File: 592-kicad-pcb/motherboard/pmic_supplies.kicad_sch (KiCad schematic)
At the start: 16 parts, among them J20 Conn_01x03, J21 Conn_01x03, J22 Conn_01x03, U21 MICROCHIP TC1304-VI0EMF, U22 LT1761ES5-BYPTRMPBF

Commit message: updates to routing
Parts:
- renumbered C39 to C42, C36 to C43, C40 to C44, C37 to C45, C38 to C46, C41 to C47, J20 to J28, J21 to J29, J22 to J30, JP5 to JP3, JP3 to JP5, R58 to R59, U21 to U22, U22 to U23
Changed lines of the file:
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@@
 		(on_board yes)
 		(dnp no)
-		(property "Reference" "U22"
+		(property "Reference" "U23"
 			(at 114.046 111.76 0)
 			(effects
@@
 			(project ""
 				(path "/5b0c97ac-fa03-4db8-b41b-0eee32b6f55d/f049e4ad-bebe-4338-850a-2727de737ae9/5cd7239b-a735-4cd0-9e02-9ed9ef16f904"
-					(reference "U22")
+					(reference "U23")
 					(unit 1)
 				)
@@
 		(on_board yes)
 		(dnp no)
-		(property "Reference" "C39"
+		(property "Reference" "C42"
 			(at 83.82 105.4035 0)
 			(effects
@@
 			(project "motherboard"
 				(path "/5b0c97ac-fa03-4db8-b41b-0eee32b6f55d/f049e4ad-bebe-4338-850a-2727de737ae9/5cd7239b-a735-4cd0-9e02-9ed9ef16f904"
-					(reference "C39")
+					(reference "C42")
 					(unit 1)
 				)
@@
 		(on_board yes)
 		(dnp no)
-		(property "Reference" "J22"
+		(property "Reference" "J30"
 			(at 199.39 105.4099 0)
 			(effects
@@
 			(project "motherboard"
 				(path "/5b0c97ac-fa03-4db8-b41b-0eee32b6f55d/f049e4ad-bebe-4338-850a-2727de737ae9/5cd7239b-a735-4cd0-9e02-9ed9ef16f904"
-					(reference "J22")
+					(reference "J30")
 					(unit 1)
 				)
@@
 		(on_board yes)
 		(dnp no)
-		(property "Reference" "C41"
+		(property "Reference" "C47"
 			(at 157.48 105.4035 0)
 			(effects
@@
 			(project "motherboard"
 				(path "/5b0c97ac-fa03-4db8-b41b-0eee32b6f55d/f049e4ad-bebe-4338-850a-2727de737ae9/5cd7239b-a735-4cd0-9e02-9ed9ef16f904"
-					(reference "C41")
+					(reference "C47")
 					(unit 1)
 				)
@@
 		(on_board yes)
 		(dnp no)
-		(property "Reference" "C40"
+		(property "Reference" "C44"
 			(at 139.7 105.4035 0)
 			(effects
@@
 			(project "motherboard"
 				(path "/5b0c97ac-fa03-4db8-b41b-0eee32b6f55d/f049e4ad-bebe-4338-850a-2727de737ae9/5cd7239b-a735-4cd0-9e02-9ed9ef16f904"
-					(reference "C40")
+					(reference "C44")
 					(unit 1)
 				)
@@
 		(on_board yes)
 		(dnp no)
-		(property "Reference" "R58"
+		(property "Reference" "R59"
 			(at 142.24 57.1499 0)
 			(effects
@@
 			(project ""
 				(path "/5b0c97ac-fa03-4db8-b41b-0eee32b6f55d/f049e4ad-bebe-4338-850a-2727de737ae9/5cd7239b-a735-4cd0-9e02-9ed9ef16f904"
-					(reference "R58")
+					(reference "R59")
 					(unit 1)
 				)
@@
 		(dnp no)
 		(fields_autoplaced yes)
-		(property "Reference" "JP5"
+		(property "Reference" "JP3"
 			(at 170.18 31.75 0)
 			(effects
@@
 			(project "motherboard"
 				(path "/5b0c97ac-fa03-4db8-b41b-0eee32b6f55d/f049e4ad-bebe-4338-850a-2727de737ae9/5cd7239b-a735-4cd0-9e02-9ed9ef16f904"
-					(reference "JP5")
+					(reference "JP3")
 					(unit 1)
 				)
@@
 		(on_board yes)
 		(dnp no)
-		(property "Reference" "C37"
+		(property "Reference" "C45"
 			(at 157.48 44.4565 0)
 			(effects
@@
 			(project "motherboard"
 				(path "/5b0c97ac-fa03-4db8-b41b-0eee32b6f55d/f049e4ad-bebe-4338-850a-2727de737ae9/5cd7239b-a735-4cd0-9e02-9ed9ef16f904"
-					(reference "C37")
+					(reference "C45")
 					(unit 1)
 				)
@@
 		(on_board yes)
 		(dnp no)
-		(property "Reference" "J21"
+		(property "Reference" "J29"
 			(at 199.39 52.0699 0)
 			(effects
@@
 			(project "motherboard"
 				(path "/5b0c97ac-fa03-4db8-b41b-0eee32b6f55d/f049e4ad-bebe-4338-850a-2727de737ae9/5cd7239b-a735-4cd0-9e02-9ed9ef16f904"
-					(reference "J21")
+					(reference "J29")
 					(unit 1)
 				)
@@
 		(on_board yes)
 		(dnp no)
-		(property "Reference" "J20"
+		(property "Reference" "J28"
 			(at 199.39 39.3699 0)
 			(effects
@@
 			(project "motherboard"
 				(path "/5b0c97ac-fa03-4db8-b41b-0eee32b6f55d/f049e4ad-bebe-4338-850a-2727de737ae9/5cd7239b-a735-4cd0-9e02-9ed9ef16f904"
-					(reference "J20")
+					(reference "J28")
 					(unit 1)
 				)
@@
 		(on_board yes)
 		(dnp no)
-		(property "Reference" "C36"
+		(property "Reference" "C43"
 			(at 86.36 39.3635 0)
 			(effects
@@
 			(project ""
 				(path "/5b0c97ac-fa03-4db8-b41b-0eee32b6f55d/f049e4ad-bebe-4338-850a-2727de737ae9/5cd7239b-a735-4cd0-9e02-9ed9ef16f904"
-					(reference "C36")
+					(reference "C43")
 					(unit 1)
 				)
@@
 		(dnp no)
 		(fields_autoplaced yes)
-		(property "Reference" "JP3"
+		(property "Reference" "JP5"
 			(at 172.72 97.79 0)
 			(effects
@@
 			(project ""
 				(path "/5b0c97ac-fa03-4db8-b41b-0eee32b6f55d/f049e4ad-bebe-4338-850a-2727de737ae9/5cd7239b-a735-4cd0-9e02-9ed9ef16f904"
-					(reference "JP3")
+					(reference "JP5")
 					(unit 1)
 				)
@@
 		(on_board yes)
 		(dnp no)
-		(property "Reference" "U21"
+		(property "Reference" "U22"
 			(at 114.3 44.958 0)
 			(effects
@@
 			(project ""
 				(path "/5b0c97ac-fa03-4db8-b41b-0eee32b6f55d/f049e4ad-bebe-4338-850a-2727de737ae9/5cd7239b-a735-4cd0-9e02-9ed9ef16f904"
-					(reference "U21")
+					(reference "U22")
 					(unit 1)
 				)
@@
 		(on_board yes)
 		(dnp no)
-		(property "Reference" "C38"
+		(property "Reference" "C46"
 			(at 157.48 54.6165 0)
 			(effects
@@
 			(project "motherboard"
 				(path "/5b0c97ac-fa03-4db8-b41b-0eee32b6f55d/f049e4ad-bebe-4338-850a-2727de737ae9/5cd7239b-a735-4cd0-9e02-9ed9ef16f904"
-					(reference "C38")
-					(unit 1)
-				)
+					(reference "C46")
+					(unit 1)
+				)

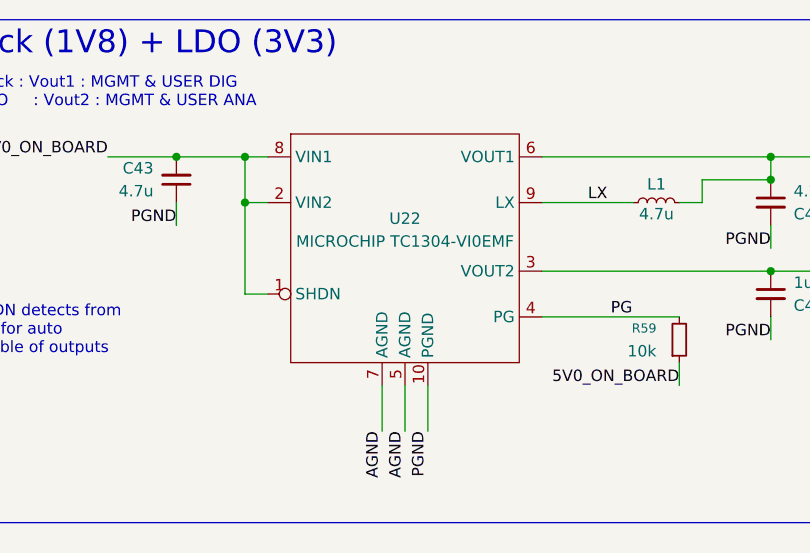
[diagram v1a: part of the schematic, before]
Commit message: update jlcpcb part numbers
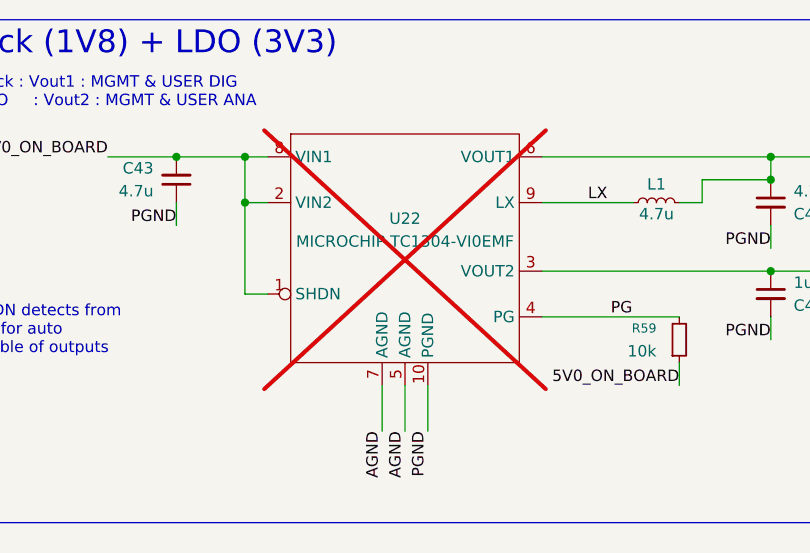
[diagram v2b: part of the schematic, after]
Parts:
- U22: now not fitted
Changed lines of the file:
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@@
 		(in_bom yes)
 		(on_board yes)
-		(dnp no)
+		(dnp yes)
 		(property "Reference" "U22"
 			(at 114.3 44.958 0)

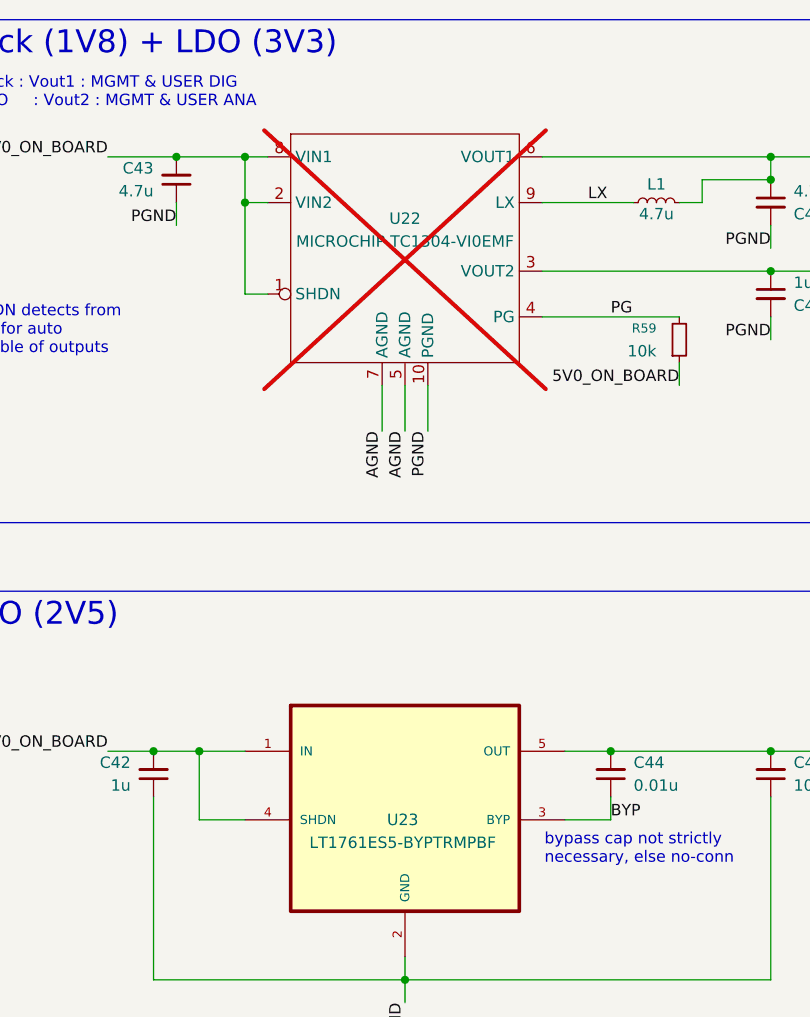
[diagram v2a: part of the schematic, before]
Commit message: can't work on one machine
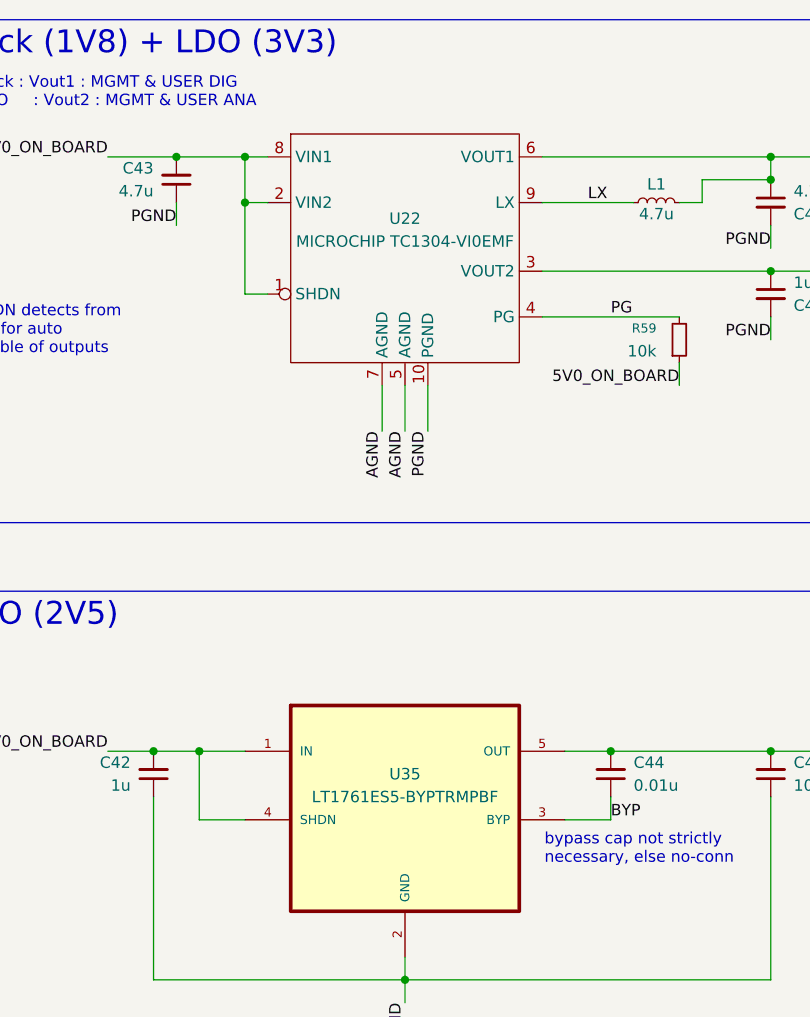
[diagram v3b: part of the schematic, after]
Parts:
- removed U23: LT1761ES5-BYPTRMPBF, LT1761ES5-BYPTRMPBF:SOT95P280X145-5N, symbol LT1761ES5-BYPTRMPBF:LT1761ES5-BYPTRMPBF
- added U35: LT1761ES5-BYPTRMPBF, LT1761ES5-BYPTRMPBF:SOT95P280X145-5N, symbol 592-partslib:LT1761ES5-BYPTRMPBF
- C43, C45: footprint (none) -> Capacitor_Tantalum_SMD:CP_EIA-3216-18_Kemet-A; LCSC (none) -> C7187
- U22: footprint (none) -> Package_DFN_QFN:DFN-10-1EP_3x3mm_P0.5mm_EP1.55x2.48mm; LCSC (none) -> C635408; now fitted; now left out of the parts list
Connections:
- net 5V0_ON_BOARD: now also U35.1 (IN), U35.4 (SHDN)
- net BYP: now also U35.3 (BYP)
- net GND: now also U35.2 (GND)
- net at C44.2, C47.2, JP5.1 (A): now also U35.5 (OUT)
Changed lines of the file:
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@@
-	)
-	(symbol
-		(lib_id "LT1761ES5-BYPTRMPBF:LT1761ES5-BYPTRMPBF")
-		(at 114.3 106.68 0)
-		(unit 1)
-		(exclude_from_sim no)
-		(in_bom yes)
-		(on_board yes)
-		(dnp no)
-		(property "Reference" "U23"
-			(at 114.046 111.76 0)
-			(effects
-				(font
-					(size 1.27 1.27)
-				)
-			)
-		)
-		(property "Value" "LT1761ES5-BYPTRMPBF"
-			(at 114.046 114.3 0)
-			(effects
-				(font
-					(size 1.27 1.27)
-				)
-			)
-		)
-		(property "Footprint" "LT1761ES5-BYPTRMPBF:SOT95P280X145-5N"
-			(at 114.3 106.68 0)
-			(effects
-				(font
-					(size 1.27 1.27)
-				)
-				(justify bottom)
-				(hide yes)
-			)
-		)
-		(property "Datasheet" "https://www.analog.com/media/en/technical-documentation/data-sheets/1761sff.pdf"
-			(at 114.3 106.68 0)
-			(effects
-				(font
-					(size 1.27 1.27)
-				)
-				(hide yes)
-			)
-		)
-		(property "Description" "Fixed 2V5 100mA LDO"
-			(at 114.3 106.68 0)
-			(effects
-				(font
-					(size 1.27 1.27)
-				)
-				(hide yes)
-			)
-		)
-		(property "MPN" "LT1761ES5-BYP#TRMPBF"
-			(at 114.3 106.68 0)
-			(effects
-				(font
-					(size 1.27 1.27)
-				)
-				(justify bottom)
-				(hide yes)
-			)
-		)
-		(property "SUPPLIER" "Linear Technology"
-			(at 114.3 106.68 0)
-			(effects
-				(font
-					(size 1.27 1.27)
-				)
-				(justify bottom)
-				(hide yes)
-			)
-		)
-		(property "OC_NEWARK" "19P0914"
-			(at 114.3 106.68 0)
-			(effects
-				(font
-					(size 1.27 1.27)
-				)
-				(justify bottom)
-				(hide yes)
-			)
-		)
-		(property "OC_FARNELL" "1663782"
-			(at 114.3 106.68 0)
-			(effects
-				(font
-					(size 1.27 1.27)
-				)
-				(justify bottom)
-				(hide yes)
-			)
-		)
-		(property "PACKAGE" "SOT-23-5"
-			(at 114.3 106.68 0)
-			(effects
-				(font
-					(size 1.27 1.27)
-				)
-				(justify bottom)
-				(hide yes)
-			)
-		)
-		(pin "4"
-		)
-		(pin "1"
-		)
-		(pin "5"
-		)
-		(pin "3"
-		)
-		(pin "2"
-		)
-		(instances
-			(project ""
-				(path "/5b0c97ac-fa03-4db8-b41b-0eee32b6f55d/f049e4ad-bebe-4338-850a-2727de737ae9/5cd7239b-a735-4cd0-9e02-9ed9ef16f904"
-					(reference "U23")
-					(unit 1)
-				)
-			)
-		)
 	)
 	(symbol
@@
 			)
 		)
-		(property "Footprint" ""
+		(property "Footprint" "Capacitor_Tantalum_SMD:CP_EIA-3216-18_Kemet-A"
 			(at 154.94 43.18 0)
 			(effects
@@
 			)
 		)
+		(property "LCSC" "C7187"
+			(at 154.94 43.18 0)
+			(effects
+				(font
+					(size 1.27 1.27)
+				)
+				(hide yes)
+			)
+		)
 		(pin "1"
 		)
@@
 				(path "/5b0c97ac-fa03-4db8-b41b-0eee32b6f55d/f049e4ad-bebe-4338-850a-2727de737ae9/5cd7239b-a735-4cd0-9e02-9ed9ef16f904"
 					(reference "J28")
+					(unit 1)
+				)
+			)
+		)
+	)
+	(symbol
+		(lib_id "592-partslib:LT1761ES5-BYPTRMPBF")
+		(at 114.3 106.68 0)
+		(unit 1)
+		(exclude_from_sim no)
+		(in_bom yes)
+		(on_board yes)
+		(dnp no)
+		(property "Reference" "U35"
+			(at 114.3 106.68 0)
+			(effects
+				(font
+					(size 1.27 1.27)
+				)
+			)
+		)
+		(property "Value" "LT1761ES5-BYPTRMPBF"
+			(at 114.3 109.22 0)
+			(effects
+				(font
+					(size 1.27 1.27)
+				)
+			)
+		)
+		(property "Footprint" "LT1761ES5-BYPTRMPBF:SOT95P280X145-5N"
+			(at 114.3 106.68 0)
+			(effects
+				(font
+					(size 1.27 1.27)
+				)
+				(justify bottom)
+				(hide yes)
+			)
+		)
+		(property "Datasheet" "https://www.analog.com/media/en/technical-documentation/data-sheets/1761sff.pdf"
+			(at 114.3 106.68 0)
+			(effects
+				(font
+					(size 1.27 1.27)
+				)
+				(hide yes)
+			)
+		)
+		(property "Description" "Fixed 2V5 100mA LDO"
+			(at 114.3 106.68 0)
+			(effects
+				(font
+					(size 1.27 1.27)
+				)
+				(hide yes)
+			)
+		)
+		(property "MPN" "LT1761ES5-BYP#TRMPBF"
+			(at 114.3 106.68 0)
+			(effects
+				(font
+					(size 1.27 1.27)
+				)
+				(justify bottom)
+				(hide yes)
+			)
+		)
+		(property "SUPPLIER" "Linear Technology"
+			(at 114.3 106.68 0)
+			(effects
+				(font
+					(size 1.27 1.27)
+				)
+				(justify bottom)
+				(hide yes)
+			)
+		)
+		(property "OC_NEWARK" "19P0914"
+			(at 114.3 106.68 0)
+			(effects
+				(font
+					(size 1.27 1.27)
+				)
+				(justify bottom)
+				(hide yes)
+			)
+		)
+		(property "OC_FARNELL" "1663782"
+			(at 114.3 106.68 0)
+			(effects
+				(font
+					(size 1.27 1.27)
+				)
+				(justify bottom)
+				(hide yes)
+			)
+		)
+		(property "PACKAGE" "SOT-23-5"
+			(at 114.3 106.68 0)
+			(effects
+				(font
+					(size 1.27 1.27)
+				)
+				(justify bottom)
+				(hide yes)
+			)
+		)
+		(pin "1"
+		)
+		(pin "4"
+		)
+		(pin "5"
+		)
+		(pin "3"
+		)
+		(pin "2"
+		)
+		(instances
+			(project ""
+				(path "/5b0c97ac-fa03-4db8-b41b-0eee32b6f55d/f049e4ad-bebe-4338-850a-2727de737ae9/5cd7239b-a735-4cd0-9e02-9ed9ef16f904"
+					(reference "U35")
 					(unit 1)
 				)
@@
 			)
 		)
-		(property "Footprint" ""
+		(property "Footprint" "Capacitor_Tantalum_SMD:CP_EIA-3216-18_Kemet-A"
 			(at 88.9 40.64 0)
 			(effects
@@
 		)
 		(property "Description" "Unpolarized capacitor, small symbol"
+			(at 88.9 40.64 0)
+			(effects
+				(font
+					(size 1.27 1.27)
+				)
+				(hide yes)
+			)
+		)
+		(property "LCSC" "C7187"
 			(at 88.9 40.64 0)
 			(effects
@@
 		(unit 1)
 		(exclude_from_sim no)
-		(in_bom yes)
-		(on_board yes)
-		(dnp yes)
+		(in_bom no)
+		(on_board yes)
+		(dnp no)
 		(property "Reference" "U22"
 			(at 114.3 44.958 0)
@@
 			)
 		)
-		(property "Footprint" ""
+		(property "Footprint" "Package_DFN_QFN:DFN-10-1EP_3x3mm_P0.5mm_EP1.55x2.48mm"
 			(at 114.3 48.26 0)
 			(effects
@@
 			(at 114.3 48.26 0)
 			(effects
+				(font
+					(size 1.27 1.27)
+				)
+				(hide yes)
+			)
+		)
+		(property "LCSC" "C635408"
+			(at 114.3 48.26 0)
+			(effects

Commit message: check in
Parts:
- U35: footprint LT1761ES5-BYPTRMPBF:SOT95P280X145-5N -> 592-partslib:SOT95P280X145-5N; LCSC (none) -> C117227
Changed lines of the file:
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@@
 			)
 		)
-		(property "Footprint" "LT1761ES5-BYPTRMPBF:SOT95P280X145-5N"
+		(property "Footprint" "592-partslib:SOT95P280X145-5N"
 			(at 114.3 106.68 0)
 			(effects
@@
 				(hide yes)
 			)
+		)
+		(property "LCSC" "C117227"
+			(at 114.3 106.68 0)
+			(effects
+				(font
+					(size 1.27 1.27)
+				)
+				(hide yes)
+			)
